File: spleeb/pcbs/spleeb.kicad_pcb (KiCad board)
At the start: 2 copper layers, 155.3 x 112.7 mm, 69 parts

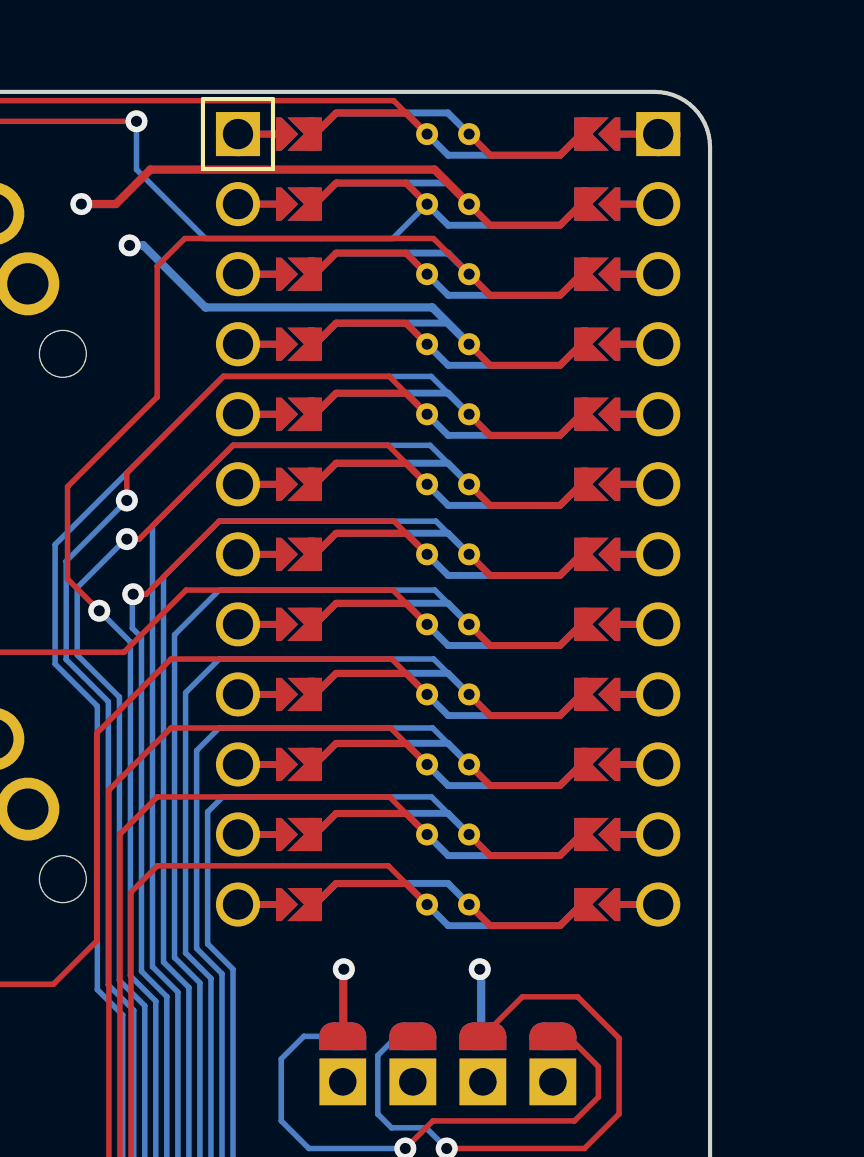
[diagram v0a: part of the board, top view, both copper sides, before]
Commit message: Address DRC errors with GND
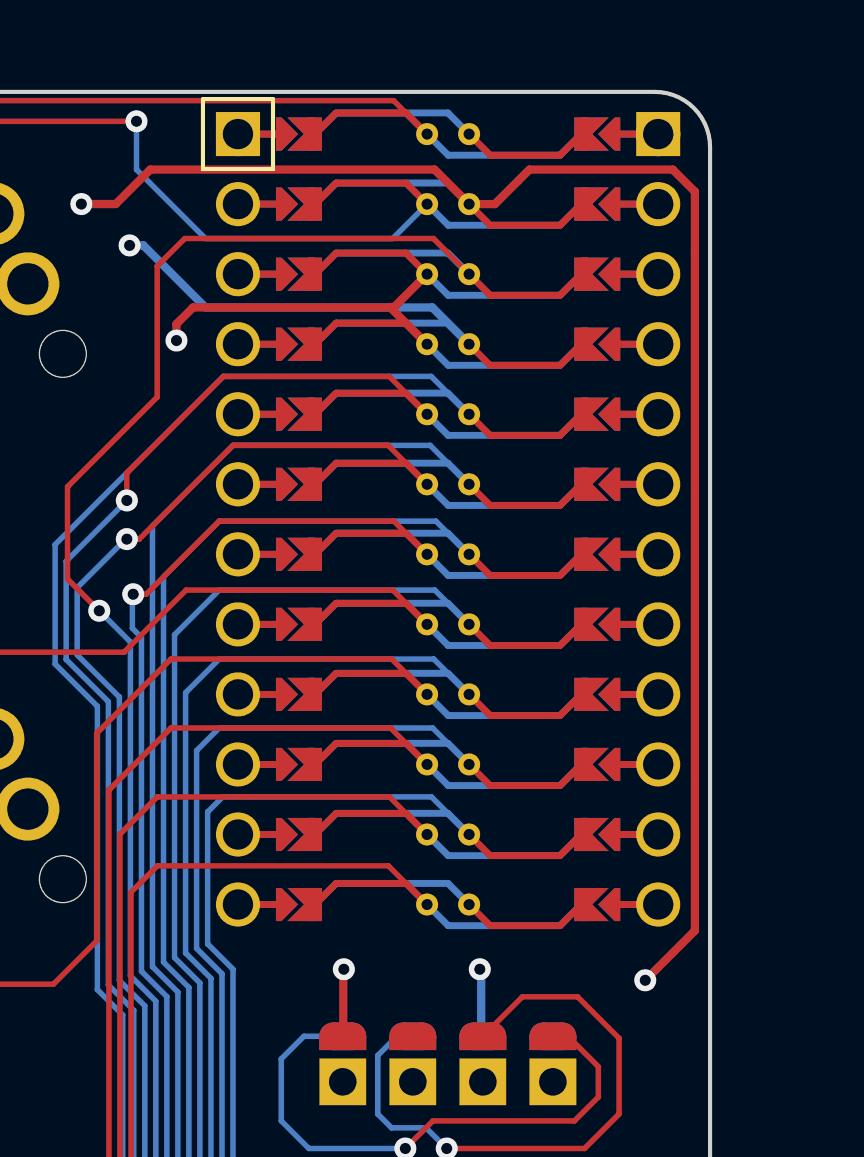
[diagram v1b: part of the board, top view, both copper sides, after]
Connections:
- D1 pad 1: outer_bottom -> P8
- D1 pad 2: outer_bottom -> P8
- D10 pad 2: ring_home -> P7
- D11 pad 1: P6 -> ring_top
- D13 pad 1: P8 -> middle_bottom
- D13 pad 2: middle_bottom -> P8
- D14 pad 1: P7 -> middle_home
- D14 pad 2: middle_home -> P7
- D15 pad 2: P6 -> middle_top
- D17 pad 1: P8 -> index_bottom
- D17 pad 2: index_bottom -> P8
- D19 pad 1: P6 -> index_top
- D19 pad 2: P6 -> index_top
- D20 pad 1: P5 -> index_number
- D20 pad 2: index_number -> P5
- D21 pad 1: inner_bottom -> P8
- D21 pad 2: P8 -> inner_bottom
- D22 pad 1: P7 -> inner_home
- D23 pad 1: inner_top -> P6
- D25 pad 1: extra_home -> P7
- D25 pad 2: P7 -> extra_home
- D26 pad 2: P6 -> extra_top
- D3 pad 2: outer_top -> P6
- D31 pad 1: P9 -> home_mods
- D31 pad 2: home_mods -> P9
- D4 pad 1: P5 -> outer_number
- D5 pad 1: P8 -> pinky_bottom
- D5 pad 2: pinky_bottom -> P8
- D7 pad 2: pinky_top -> P6
- D8 pad 2: pinky_number -> P5
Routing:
- net GND: track 17.6 -> 68.3 mm, vias 2 -> 4

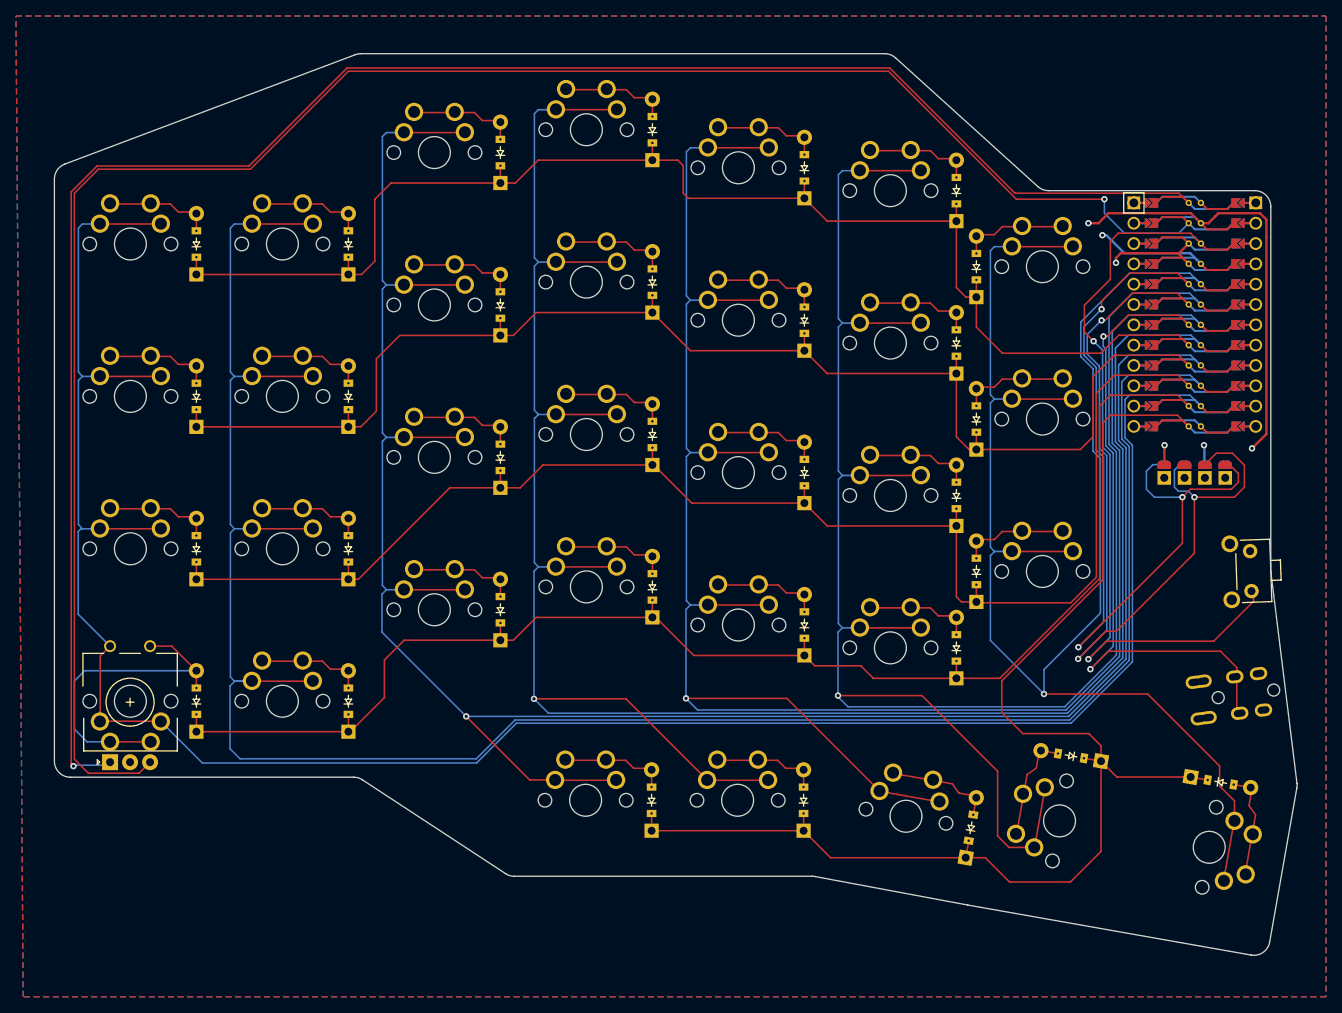
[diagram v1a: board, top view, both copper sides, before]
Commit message: Replace jumper pad promicro footprint with reversable thru hole footprint to allow standoffs for oled
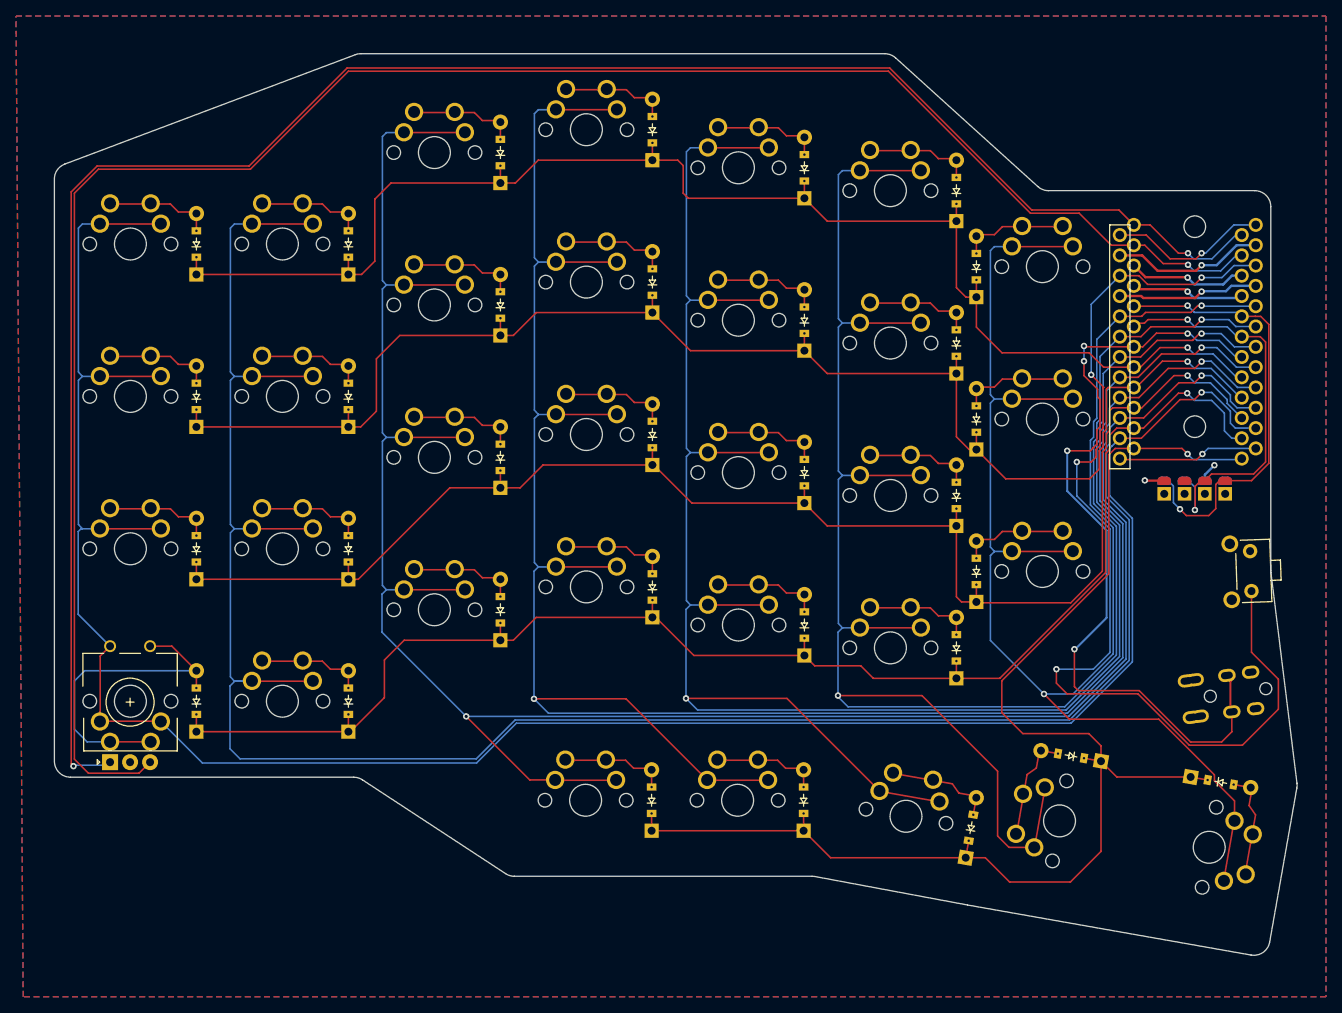
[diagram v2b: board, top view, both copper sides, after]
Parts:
- removed REF**: TRRS-PJ-320A-dual, TRRS-PJ-320A-dual
- added MP1: , Hole, F.Cu at (133.1, -59.3)
- added MP2: , Hole, F.Cu at (133.1, -34.3)
- added TRRS1: TRRS-PJ-320A-dual, TRRS-PJ-320A-dual, F.Cu at (143.8, 0.50)
- MCU1: moved to B.Cu
- moved MCU1 2.75 mm to (133.1, -45.6)
- moved OLED1 2.00 mm to (127.0, -24.3)
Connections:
- D1 pad 1: P8 -> outer_bottom
- D1 pad 2: P8 -> outer_bottom
- D11 pad 1: ring_top -> P6
- D11 pad 2: P6 -> ring_top
- D12 pad 1: ring_number -> P5
- D12 pad 2: ring_number -> P5
- D13 pad 2: P8 -> middle_bottom
- D14 pad 1: middle_home -> P7
- D16 pad 2: P5 -> middle_number
- D18 pad 1: index_home -> P7
- D19 pad 2: index_top -> P6
- D20 pad 1: index_number -> P5
- D22 pad 2: P7 -> inner_home
- D23 pad 1: P6 -> inner_top
- D23 pad 2: inner_top -> P6
- D24 pad 2: P5 -> inner_number
- D25 pad 1: P7 -> extra_home
- D25 pad 2: extra_home -> P7
- D26 pad 1: P6 -> extra_top
- D29 pad 2: P9 -> mod_two_mods
- D32 pad 1: far_mods -> P9
- D32 pad 2: P9 -> far_mods
- D4 pad 2: outer_number -> P5
- D5 pad 2: P8 -> pinky_bottom
- D6 pad 2: P7 -> pinky_home
- D7 pad 2: P6 -> pinky_top
- D8 pad 1: pinky_number -> P5
- D8 pad 2: P5 -> pinky_number
- MCU1 pad 13: P9 -> P1
- MCU1 pad 14: P8 -> P0
- MCU1 pad 15: P7 -> GND
- MCU1 pad 16: P6 -> GND
- MCU1 pad 17: P5 -> P2
- MCU1 pad 18: P4 -> P3
- MCU1 pad 19: P3 -> P4
- MCU1 pad 20: P2 -> P5
- MCU1 pad 21: GND -> P6
- MCU1 pad 22: GND -> P7
- MCU1 pad 23: P0 -> P8
- MCU1 pad 24: P1 -> P9
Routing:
- net P3: track 107.8 -> 50.5 mm, vias 3 -> 2
- net P2: track 104.2 -> 55.8 mm, vias 3 -> 2
- net RST: track 93.2 -> 130.1 mm, vias 2 -> 4
- net P4: track 80.8 -> 102.5 mm, vias 2 -> 5
- net RAW: track 0.00 -> 20.0 mm, vias 0 -> 1
- net GND: track 68.3 -> 50.7 mm
- net P10: track 0.00 -> 17.6 mm, vias 0 -> 1
- net P6: track 172.8 -> 184.5 mm, vias 0 -> 1
- net P1: track 229.8 -> 240.5 mm, vias 1 -> 2
- net P5: track 172.5 -> 181.0 mm, vias 0 -> 1
- net P16: track 267.7 -> 276.1 mm, vias 0 -> 1
- net P0: track 237.0 -> 244.9 mm
- net P14: track 265.0 -> 272.6 mm, vias 0 -> 1
- net P8: track 178.7 -> 185.6 mm, vias 0 -> 1
- net P15: track 265.1 -> 271.6 mm, vias 1 -> 2
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
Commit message: Updates for plate including oled cutout
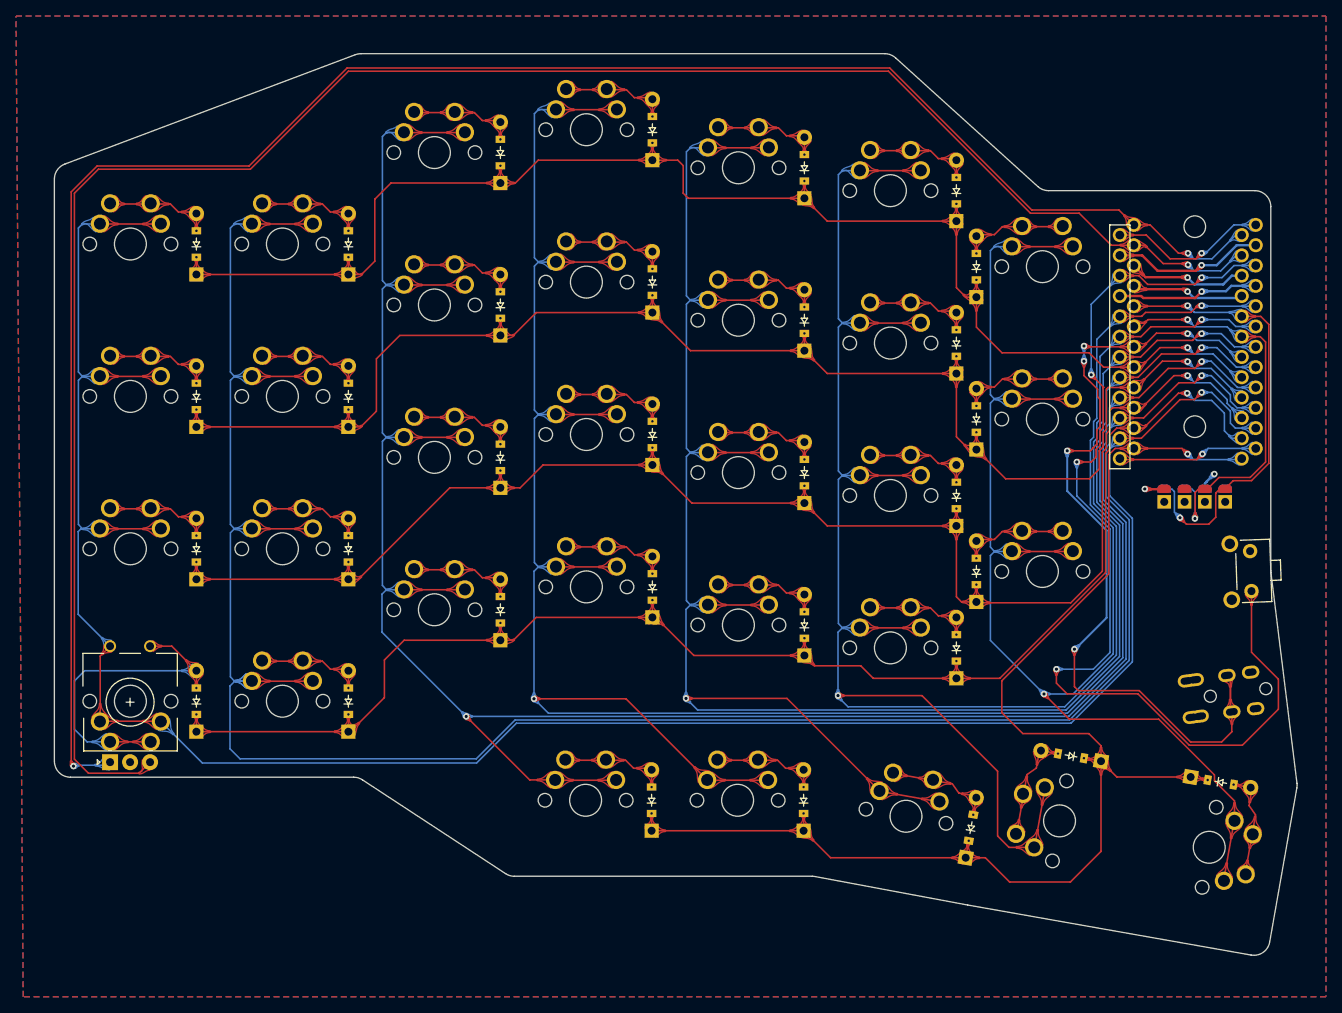
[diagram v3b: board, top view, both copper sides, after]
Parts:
- moved OLED1 1.00 mm to (127.0, -23.3)
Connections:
- D1 pad 2: outer_bottom -> P8
- D10 pad 2: P7 -> ring_home
- D11 pad 1: P6 -> ring_top
- D12 pad 2: P5 -> ring_number
- D14 pad 2: P7 -> middle_home
- D15 pad 1: P6 -> middle_top
- D15 pad 2: middle_top -> P6
- D17 pad 2: P8 -> index_bottom
- D2 pad 1: P7 -> outer_home
- D20 pad 1: P5 -> index_number
- D22 pad 1: inner_home -> P7
- D22 pad 2: inner_home -> P7
- D23 pad 1: inner_top -> P6
- D24 pad 2: inner_number -> P5
- D25 pad 1: extra_home -> P7
- D26 pad 1: extra_top -> P6
- D26 pad 2: extra_top -> P6
- D27 pad 2: P5 -> extra_number
- D28 pad 1: P9 -> mod_one_mods
- D28 pad 2: mod_one_mods -> P9
- D30 pad 1: P9 -> near_mods
- D4 pad 2: P5 -> outer_number
- D5 pad 2: pinky_bottom -> P8
- D6 pad 1: P7 -> pinky_home
- D7 pad 1: P6 -> pinky_top
- D8 pad 2: pinky_number -> P5
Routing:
- net P3: track 50.5 -> 51.4 mm
- net P2: track 55.8 -> 56.5 mm
